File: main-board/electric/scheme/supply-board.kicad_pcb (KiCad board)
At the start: 2 copper layers, 85 x 56 mm, 141 parts, among them K1 CONN_3, P1 CONN_13X2, P1 PWR-IN, P10 TST, P11 TST, P12 PWR-IN, P13 CONN_4, P14 PWR-IN, P15 CONN_4, P16 TST, P17 TST, P18 TST, P19 TST, P2 PWR-IN, P3 CONN_4, P4 CONN_10, P5 PWR-IN, P6 TST, P7 TST, P8 TST, P9 CONN_3X2, Q1 BC847, Q10 MOS_N, Q11 MOS_P, Q12 MOS_P, Q2 BC847, Q3 BC847, Q4 MOS_P, Q5 BC847, Q6 BC857, Q7 BC847, Q8 BC857, Q9 BC847, U1 NCP3063, U2 L293, U3 MINI-USB-B, X1 8MHz

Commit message: Placing components...
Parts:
- moved R29 199.3 mm to (78.0, 146.0), turned to 270 degrees
- moved R27 198.3 mm to (82.0, 146.0), turned to 270 degrees
- moved C10 195.4 mm to (72.0, 147.0), turned to 90 degrees
- moved R26 190.5 mm to (76.0, 145.0), turned to 270 degrees
- moved R30 189.9 mm to (72.0, 143.0), turned to 270 degrees
- moved R33 185.4 mm to (87.0, 127.0), turned to 90 degrees
- moved R34 185.4 mm to (87.0, 131.0), turned to 90 degrees
- moved C12 185.1 mm to (61.0, 145.0), turned to 90 degrees
- moved R43 182.4 mm to (50.0, 147.0), turned to 270 degrees
- moved R37 182.3 mm to (59.0, 145.0), turned to 270 degrees
- moved R35 180.0 mm to (80.0, 132.0)
- moved R28 179.6 mm to (61.0, 141.0), turned to 270 degrees
- moved R36 178.6 mm to (76.0, 132.0)
- moved R32 178.5 mm to (65.0, 142.0), turned to 180 degrees
- moved R31 177.9 mm to (51.0, 142.0), turned to 270 degrees
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
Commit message: Placing elements.
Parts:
- removed the P1 at (161.0, 129.0)
- removed P15: CONN_4, PIN_ARRAY_4x1
- C17, C18, C20, C6, C7, Q11, Q3, Q5, Q6, R51, R54, R60: moved to B.Cu
- R12, R13: value 10k -> 30k
- moved P8 281.1 mm to (193.0, 184.0)
- moved P6 278.6 mm to (191.0, 184.5)
- moved P7 274.6 mm to (188.5, 185.0)
- moved P3 274.5 mm to (201.5, 178.5)
- moved R9 271.7 mm to (172.5, 175.0), turned to 270 degrees
- moved R5 271.3 mm to (170.0, 175.0), turned to 90 degrees
- moved P5 258.1 mm to (171.0, 178.5), turned to 180 degrees
- moved D2 255.9 mm to (146.5, 219.5)
- moved D1 255.8 mm to (140.5, 219.5)
- moved K1 255.1 mm to (178.5, 178.5)
- moved R2 254.5 mm to (140.5, 215.0)
- moved R4 242.5 mm to (149.0, 169.5), turned to 180 degrees
- moved X1 241.2 mm to (189.0, 150.5)
- moved R8 238.5 mm to (146.0, 215.0)
- moved R7 238.2 mm to (149.0, 167.0), turned to 180 degrees
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
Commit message: Placing components...
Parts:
- C18: moved to F.Cu
- Q10, Q2, Q7, Q8, R50, R56, R59: moved to B.Cu
- moved R45 196.6 mm to (91.0, 141.5)
- moved R44 190.7 mm to (87.5, 141.5)
- moved C16 173.2 mm to (80.5, 134.5), turned to 180 degrees
- moved C19 170.2 mm to (85.5, 107.5), turned to 270 degrees
- moved C15 169.3 mm to (79.5, 137.5), turned to 180 degrees
- moved C22 163.7 mm to (87.5, 107.5), turned to 270 degrees
- moved R59 156.0 mm to (83.5, 109.0), turned to 90 degrees
- moved Q7 155.3 mm to (78.5, 112.5), turned to 90 degrees
- moved R70 155.1 mm to (88.0, 100.0), turned to 90 degrees
- moved R69 154.7 mm to (88.0, 103.5), turned to 90 degrees
- moved R50 152.0 mm to (76.5, 105.0), turned to 90 degrees
- moved R56 150.6 mm to (80.0, 109.0), turned to 90 degrees
- moved Q8 144.4 mm to (82.5, 113.0), turned to 180 degrees
- moved Q10 143.9 mm to (81.5, 102.5), turned to 180 degrees
- moved Q2 140.0 mm to (77.0, 109.0), turned to 90 degrees
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
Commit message: Placing components...
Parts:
- moved R47 154.6 mm to (68.0, 112.0), turned to 270 degrees
- moved R46 152.8 mm to (68.0, 108.5), turned to 270 degrees
- moved C15 18.1 mm to (63.5, 129.0)
- moved R45 16.0 mm to (85.5, 126.5), turned to 90 degrees
- moved C17 15.6 mm to (75.0, 118.5)
- moved C20 15.6 mm to (75.0, 116.0)
- moved D5 15.6 mm to (77.0, 127.0)
- moved L3 15.6 mm to (72.0, 113.5)
- moved Q11 15.6 mm to (72.0, 124.5)
- moved Q3 15.6 mm to (72.5, 109.0)
- moved Q5 15.6 mm to (70.0, 114.5)
- moved Q6 15.6 mm to (74.5, 113.0)
- moved R51 15.6 mm to (72.5, 106.0)
- moved R54 15.6 mm to (70.0, 111.5)
- moved R60 15.6 mm to (70.0, 118.0)
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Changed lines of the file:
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@@
   )
   (module SOT23EBC (layer B.Cu)
-    (at 60.5 119 180)
+    (at 72.5 109 180)
     (descr "Module CMS SOT23 Transistore EBC")
     (tags "CMS SOT")
@@
   )
   (module SOT23EBC (layer B.Cu)
-    (at 58 124.5 90)
+    (at 70 114.5 90)
     (descr "Module CMS SOT23 Transistore EBC")
     (tags "CMS SOT")
@@
   )
   (module SOT23EBC (layer B.Cu)
-    (at 62.5 123 270)
+    (at 74.5 113 270)
     (descr "Module CMS SOT23 Transistore EBC")
     (tags "CMS SOT")
@@
   )
   (module SM0805 (layer B.Cu)
-    (at 63 126)
+    (at 75 116)
     (attr smd)
     (fp_text reference C20 (at 0 0.3175) (layer B.SilkS)
@@
   )
   (module SM0805 (layer F.Cu)
-    (at -32.5 -5.5)
+    (at 68 112 270)
     (attr smd)
-    (fp_text reference R47 (at 0 -0.3175) (layer F.SilkS)
+    (fp_text reference R47 (at 0 -0.3175 270) (layer F.SilkS)
       (effects (font (size 0.50038 0.50038) (thickness 0.10922)))
     )
-    (fp_text value 10k (at 0 0.381) (layer F.SilkS)
+    (fp_text value 10k (at 0 0.381 270) (layer F.SilkS)
       (effects (font (size 0.50038 0.50038) (thickness 0.10922)))
     )
@@
     (fp_line (start 1.524 -0.762) (end 1.524 0.762) (layer F.SilkS) (width 0.09906))
     (fp_line (start 1.524 0.762) (end 0.508 0.762) (layer F.SilkS) (width 0.09906))
-    (pad 1 smd rect (at -0.9525 0) (size 0.889 1.397)
+    (pad 1 smd rect (at -0.9525 0 270) (size 0.889 1.397)
       (layers F.Cu F.Paste F.Mask)
       (net 10 /buck-volt)
     )
-    (pad 2 smd rect (at 0.9525 0) (size 0.889 1.397)
+    (pad 2 smd rect (at 0.9525 0 270) (size 0.889 1.397)
       (layers F.Cu F.Paste F.Mask)
       (net 43 GND)
@@
   )
   (module SM0805 (layer F.Cu)
-    (at -36 -3.5)
+    (at 68 108.5 270)
     (attr smd)
-    (fp_text reference R46 (at 0 -0.3175) (layer F.SilkS)
+    (fp_text reference R46 (at 0 -0.3175 270) (layer F.SilkS)
       (effects (font (size 0.50038 0.50038) (thickness 0.10922)))
     )
-    (fp_text value 68k (at 0 0.381) (layer F.SilkS)
+    (fp_text value 68k (at 0 0.381 270) (layer F.SilkS)
       (effects (font (size 0.50038 0.50038) (thickness 0.10922)))
     )
@@
     (fp_line (start 1.524 -0.762) (end 1.524 0.762) (layer F.SilkS) (width 0.09906))
     (fp_line (start 1.524 0.762) (end 0.508 0.762) (layer F.SilkS) (width 0.09906))
-    (pad 1 smd rect (at -0.9525 0) (size 0.889 1.397)
+    (pad 1 smd rect (at -0.9525 0 270) (size 0.889 1.397)
       (layers F.Cu F.Paste F.Mask)
       (net 8 /buck-out-5v)
     )
-    (pad 2 smd rect (at 0.9525 0) (size 0.889 1.397)
+    (pad 2 smd rect (at 0.9525 0 270) (size 0.889 1.397)
       (layers F.Cu F.Paste F.Mask)
       (net 10 /buck-volt)
@@
   )
   (module SM0805 (layer B.Cu)
-    (at 63 128.5)
+    (at 75 118.5)
     (attr smd)
     (fp_text reference C17 (at 0 0.3175) (layer B.SilkS)
@@
   )
   (module SM0805 (layer B.Cu)
-    (at 60.5 116)
+    (at 72.5 106)
     (attr smd)
     (fp_text reference R51 (at 0 0.3175) (layer B.SilkS)
@@
   )
   (module SM0805 (layer B.Cu)
-    (at 58 128 270)
+    (at 70 118 270)
     (attr smd)
     (fp_text reference R60 (at 0 0.3175 270) (layer B.SilkS)
@@
   )
   (module SM0805 (layer B.Cu)
-    (at 58 121.5)
+    (at 70 111.5)
     (attr smd)
     (fp_text reference R54 (at 0 0.3175) (layer B.SilkS)
@@
   )
   (module SM0805 (layer F.Cu)
-    (at 61 103.5)
+    (at 68 96 180)
     (attr smd)
-    (fp_text reference C18 (at 0 -0.3175) (layer F.SilkS)
+    (fp_text reference C18 (at 0 -0.3175 180) (layer F.SilkS)
       (effects (font (size 0.50038 0.50038) (thickness 0.10922)))
     )
-    (fp_text value 100n (at 0 0.381) (layer F.SilkS)
+    (fp_text value 100n (at 0 0.381 180) (layer F.SilkS)
       (effects (font (size 0.50038 0.50038) (thickness 0.10922)))
     )
@@
     (fp_line (start 1.524 -0.762) (end 1.524 0.762) (layer F.SilkS) (width 0.09906))
     (fp_line (start 1.524 0.762) (end 0.508 0.762) (layer F.SilkS) (width 0.09906))
-    (pad 1 smd rect (at -0.9525 0) (size 0.889 1.397)
+    (pad 1 smd rect (at -0.9525 0 180) (size 0.889 1.397)
       (layers F.Cu F.Paste F.Mask)
       (net 8 /buck-out-5v)
     )
-    (pad 2 smd rect (at 0.9525 0) (size 0.889 1.397)
+    (pad 2 smd rect (at 0.9525 0 180) (size 0.889 1.397)
       (layers F.Cu F.Paste F.Mask)
       (net 43 GND)
@@
   )
   (module SM0805 (layer F.Cu)
-    (at 91 141.5)
+    (at 85.5 126.5 90)
     (attr smd)
-    (fp_text reference R45 (at 0 -0.3175) (layer F.SilkS)
+    (fp_text reference R45 (at 0 -0.3175 90) (layer F.SilkS)
       (effects (font (size 0.50038 0.50038) (thickness 0.10922)))
     )
-    (fp_text value 10k (at 0 0.381) (layer F.SilkS)
+    (fp_text value 10k (at 0 0.381 90) (layer F.SilkS)
       (effects (font (size 0.50038 0.50038) (thickness 0.10922)))
     )
@@
     (fp_line (start 1.524 -0.762) (end 1.524 0.762) (layer F.SilkS) (width 0.09906))
     (fp_line (start 1.524 0.762) (end 0.508 0.762) (layer F.SilkS) (width 0.09906))
-    (pad 1 smd rect (at -0.9525 0) (size 0.889 1.397)
+    (pad 1 smd rect (at -0.9525 0 90) (size 0.889 1.397)
       (layers F.Cu F.Paste F.Mask)
       (net 37 /solar-volt)
     )
-    (pad 2 smd rect (at 0.9525 0) (size 0.889 1.397)
+    (pad 2 smd rect (at 0.9525 0 90) (size 0.889 1.397)
       (layers F.Cu F.Paste F.Mask)
       (net 43 GND)
@@
   )
   (module SM0805 (layer F.Cu)
-    (at 87.5 141.5)
+    (at 85.5 130.5 90)
     (attr smd)
-    (fp_text reference R44 (at 0 -0.3175) (layer F.SilkS)
+    (fp_text reference R44 (at 0 -0.3175 90) (layer F.SilkS)
       (effects (font (size 0.50038 0.50038) (thickness 0.10922)))
     )
-    (fp_text value 68k (at 0 0.381) (layer F.SilkS)
+    (fp_text value 68k (at 0 0.381 90) (layer F.SilkS)
       (effects (font (size 0.50038 0.50038) (thickness 0.10922)))
     )
@@
     (fp_line (start 1.524 -0.762) (end 1.524 0.762) (layer F.SilkS) (width 0.09906))
     (fp_line (start 1.524 0.762) (end 0.508 0.762) (layer F.SilkS) (width 0.09906))
-    (pad 1 smd rect (at -0.9525 0) (size 0.889 1.397)
+    (pad 1 smd rect (at -0.9525 0 90) (size 0.889 1.397)
       (layers F.Cu F.Paste F.Mask)
       (net 35 /solar)
     )
-    (pad 2 smd rect (at 0.9525 0) (size 0.889 1.397)
+    (pad 2 smd rect (at 0.9525 0 90) (size 0.889 1.397)
       (layers F.Cu F.Paste F.Mask)
       (net 37 /solar-volt)
@@
   )
   (module SM0805 (layer F.Cu)
-    (at 80.5 134.5 180)
+    (at 79.5 132.5 270)
     (attr smd)
-    (fp_text reference C16 (at 0 -0.3175 180) (layer F.SilkS)
+    (fp_text reference C16 (at 0 -0.3175 270) (layer F.SilkS)
       (effects (font (size 0.50038 0.50038) (thickness 0.10922)))
     )
-    (fp_text value 100n (at 0 0.381 180) (layer F.SilkS)
+    (fp_text value 100n (at 0 0.381 270) (layer F.SilkS)
       (effects (font (size 0.50038 0.50038) (thickness 0.10922)))
     )
@@
     (fp_line (start 1.524 -0.762) (end 1.524 0.762) (layer F.SilkS) (width 0.09906))
     (fp_line (start 1.524 0.762) (end 0.508 0.762) (layer F.SilkS) (width 0.09906))
-    (pad 1 smd rect (at -0.9525 0 180) (size 0.889 1.397)
+    (pad 1 smd rect (at -0.9525 0 270) (size 0.889 1.397)
       (layers F.Cu F.Paste F.Mask)
       (net 35 /solar)
     )
-    (pad 2 smd rect (at 0.9525 0 180) (size 0.889 1.397)
+    (pad 2 smd rect (at 0.9525 0 270) (size 0.889 1.397)
       (layers F.Cu F.Paste F.Mask)
       (net 43 GND)
@@
   )
   (module D3 (layer F.Cu)
-    (at 65 137 270)
+    (at 77 127 270)
     (descr "Diode 3 pas")
     (tags "DIODE DEV")
@@
   )
   (module C2V10 (layer F.Cu)
-    (at 62.5 100)
+    (at 63.5 101 180)
     (descr "Condensateur polarise")
     (tags CP)
-    (fp_text reference C21 (at 0 2.54) (layer F.SilkS)
+    (fp_text reference C21 (at 0 2.54 180) (layer F.SilkS)
       (effects (font (size 1.27 1.27) (thickness 0.254)))
     )
-    (fp_text value 1m (at 0 -2.54) (layer F.SilkS)
+    (fp_text value 1m (at 0 -2.54 180) (layer F.SilkS)
       (effects (font (size 1.27 1.27) (thickness 0.254)))
     )
     (fp_circle (center 0 0) (end 4.826 -2.794) (layer F.SilkS) (width 0.3048))
-    (pad 1 thru_hole rect (at -2.54 0) (size 1.778 1.778) (drill 1.016)
+    (pad 1 thru_hole rect (at -2.54 0 180) (size 1.778 1.778) (drill 1.016)
       (layers *.Cu *.Mask F.SilkS)
       (net 8 /buck-out-5v)
     )
-    (pad 2 thru_hole circle (at 2.54 0) (size 1.778 1.778) (drill 1.016)
+    (pad 2 thru_hole circle (at 2.54 0 180) (size 1.778 1.778) (drill 1.016)
       (layers *.Cu *.Mask F.SilkS)
       (net 43 GND)
@@
   )
   (module C2V10 (layer F.Cu)
-    (at 79.5 137.5 180)
+    (at 63.5 129 180)
     (descr "Condensateur polarise")
     (tags CP)
@@
   )
   (module SOT223-GDSD (layer B.Cu)
-    (at 60 134.5)
+    (at 72 124.5)
     (descr "module CMS SOT223 4 pins")
     (tags "CMS SOT")
@@
   )
   (module inductance_25mH_3A (layer F.Cu)
-    (at 60 123.5 90)
+    (at 72 113.5 90)
     (fp_text reference L3 (at 0 -1.6 90) (layer F.SilkS)
       (effects (font (size 1 1) (thickness 0.15)))

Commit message: Placing components...
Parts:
- C16, C18, C19, C22, R44, R45, R46, R47, R69, R70: moved to B.Cu
- moved C18 62.6 mm to (110.5, 142.0), turned to 270 degrees
- moved C15 57.7 mm to (102.0, 172.0)
- moved C17 57.7 mm to (113.5, 161.5)
- moved C19 57.7 mm to (124.0, 150.5)
- moved C20 57.7 mm to (113.5, 159.0)
- moved C21 57.7 mm to (102.0, 144.0)
- moved C22 57.7 mm to (126.0, 150.5)
- moved D5 57.7 mm to (115.5, 170.0)
- moved D6 57.7 mm to (124.0, 143.5)
- moved L2 57.7 mm to (120.0, 157.0)
- moved L3 57.7 mm to (110.5, 156.5)
- moved Q10 57.7 mm to (120.0, 145.5)
- moved Q11 57.7 mm to (110.5, 167.5)
- moved Q2 57.7 mm to (115.5, 152.0)
- moved Q3 57.7 mm to (111.0, 152.0)
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
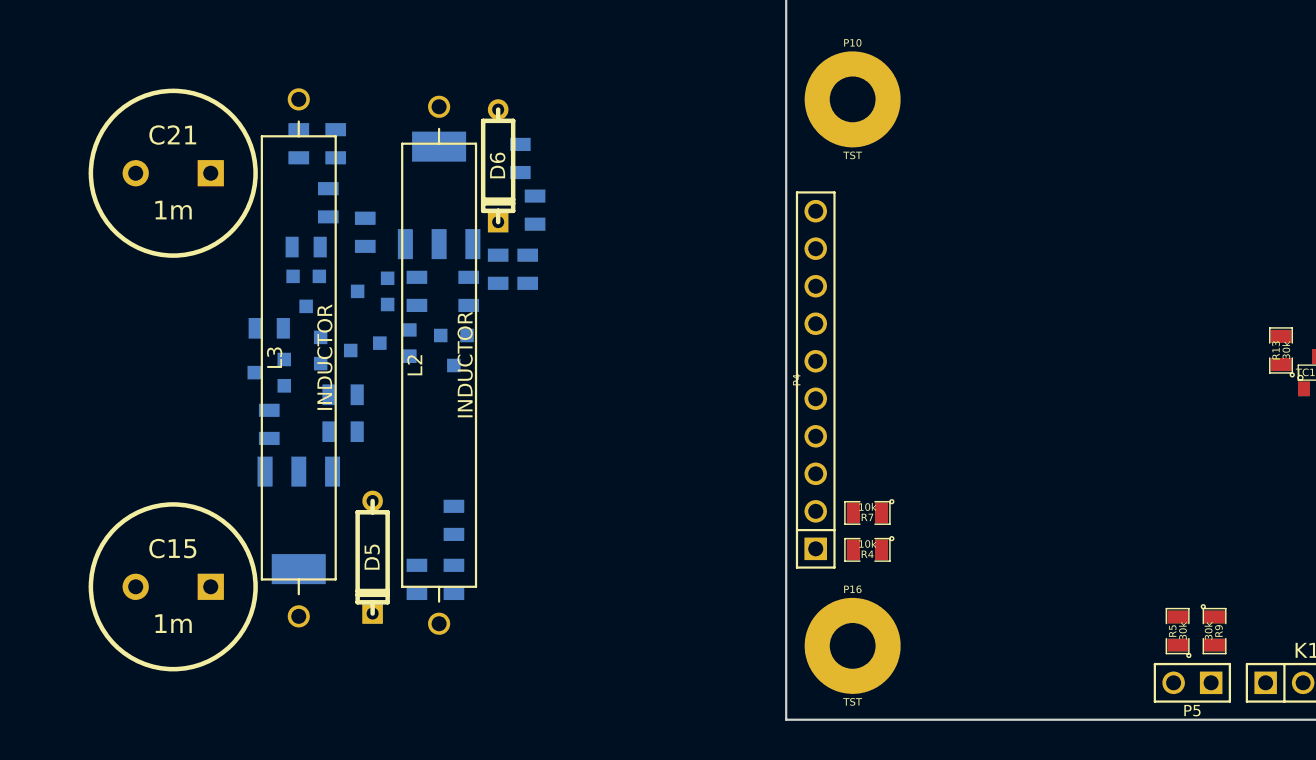
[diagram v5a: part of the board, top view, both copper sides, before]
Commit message: Placing elements.
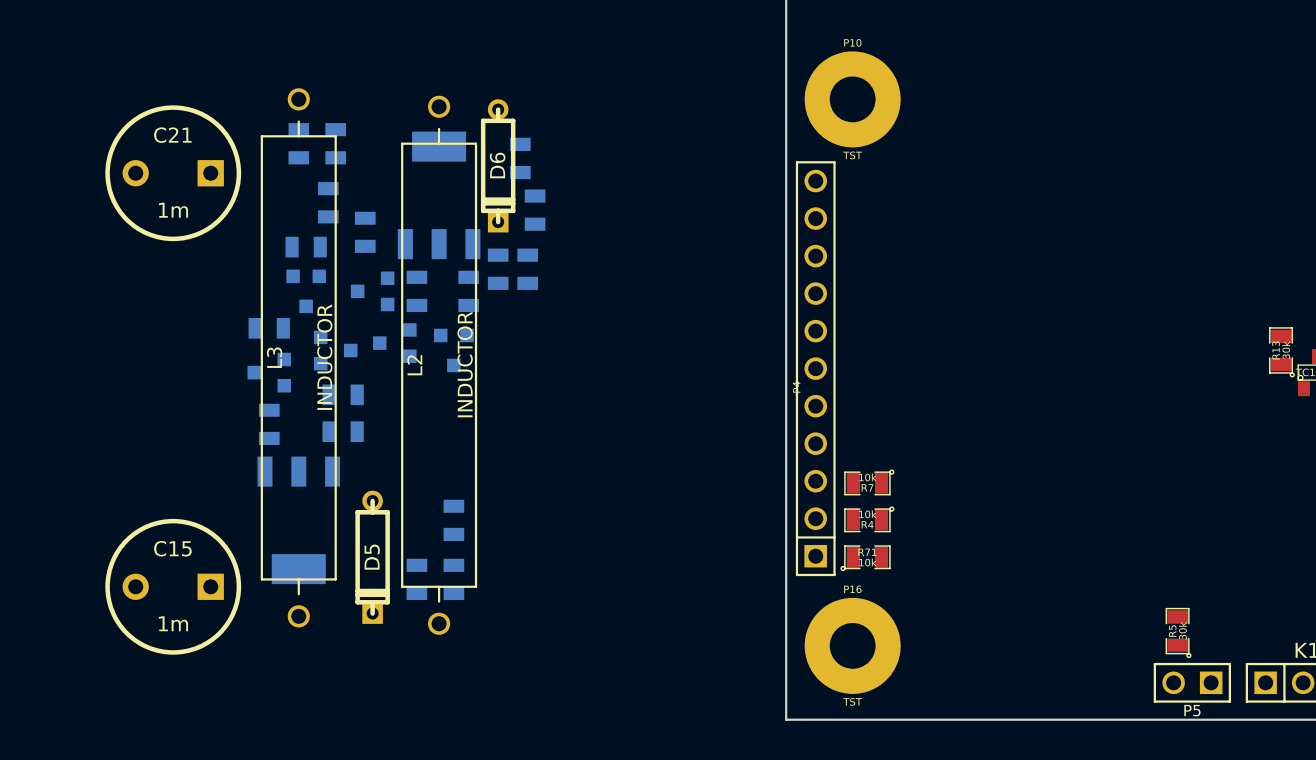
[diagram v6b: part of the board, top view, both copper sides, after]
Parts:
- removed R9: 30k, SM0805
- added R71: 10k, SM0805, F.Cu at (149.0, 170.0)
- C15, C21: footprint C2V10 -> C2V8
- P4: value CONN_10 -> cross board conn; footprint PIN_ARRAY-10X1 -> PIN_ARRAY-11X1
- moved R4 2.00 mm to (149.0, 167.5)
- moved R7 2.00 mm to (149.0, 165.0)
- moved P4 0.50 mm to (145.5, 158.5)
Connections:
- P4 pad 1: /sda-int -> N-0000040
- P4 pad 2: /scl-int -> /sda-int
- P4 pad 3: GND -> /scl-int
- P4 pad 5: VDD -> GND
- P4 pad 7: +6V -> VDD
- P4 pad 9: /buck-out-5v -> +6V
- P5 pad 1: N-0000089 -> /just-power-source
- R5 pad 1: N-0000089 -> /just-power-source
- stm1 pad 19: (no net) -> /wakeup

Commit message: Placing elements.
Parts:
- Q1, Q12, Q4, Q9, R48, R49, R52, R53, R55, R57, R58, R61: moved to B.Cu
- moved R48 290.4 mm to (205.5, 156.5), turned to 270 degrees
- moved R53 287.6 mm to (208.5, 148.5), turned to 90 degrees
- moved R49 286.4 mm to (208.5, 156.5), turned to 90 degrees
- moved R52 266.4 mm to (206.0, 148.5), turned to 270 degrees
- moved Q4 247.0 mm to (207.5, 144.5)
- moved Q1 246.1 mm to (207.0, 152.5)
- moved U2 245.9 mm to (205.5, 149.0), turned to 90 degrees
- moved R61 145.5 mm to (200.5, 172.5)
- moved P12 143.6 mm to (204.0, 175.0), turned to 180 degrees
- moved R64 143.5 mm to (205.5, 171.5), turned to 270 degrees
- moved Q12 142.3 mm to (204.5, 171.5), turned to 270 degrees
- moved R63 141.0 mm to (203.5, 171.5), turned to 270 degrees
- moved R62 138.5 mm to (201.5, 171.5), turned to 270 degrees
- moved Q9 137.9 mm to (199.5, 167.0), turned to 180 degrees
- moved R58 137.4 mm to (200.5, 170.0)
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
